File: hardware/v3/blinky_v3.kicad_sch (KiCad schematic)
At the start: 147 parts, among them J1 Conn_01x07, J2 Conn_01x03_Pin, J3 RJ45, J4 Conn_01x06_Pin, J5 Conn_01x05_Pin, J6 Conn_02x10_Counter_Clockwise, J7 Conn_01x04_Pin, J8 Conn_01x04_Pin, J9 Conn_01x06_Pin, Q1 2N7002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

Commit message: start routing
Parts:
- J6: now not fitted; now left out of the parts list
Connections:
- net OCXO_OUT: now reaches JP11.1 (A), JP13.1 (A), TP12.1, Y2.4 (RF_OUTPUT)
- net 10Mhz2.5V: now reaches C10.2, R25.2, R4.1, TP6.1, U14.6 (-), U4.3 (+)
- net 10MHz0v: now reaches C40.2, R38.1, TP21.1, U2.3 (+), U3.3 (+IN)
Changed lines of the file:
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@@
     (effects (font (size 1.27 1.27)) (justify left bottom))
   )
+  (label "OCXO_OUT" (at 86.36 259.08 0) (fields_autoplaced)
+    (effects (font (size 1.27 1.27)) (justify left bottom))
+  )
   (label "LEDM3" (at 312.42 55.88 0) (fields_autoplaced)
     (effects (font (size 1.27 1.27)) (justify left bottom))
   )
+  (label "10Mhz2.5V" (at 119.38 232.41 0) (fields_autoplaced)
+    (effects (font (size 1.27 1.27)) (justify left bottom))
+  )
   (label "LEDB" (at 312.42 86.36 0) (fields_autoplaced)
     (effects (font (size 1.27 1.27)) (justify left bottom))
@@
     (effects (font (size 1.27 1.27)) (justify left bottom))
   )
+  (label "10MHz0v" (at 119.38 281.94 0) (fields_autoplaced)
+    (effects (font (size 1.27 1.27)) (justify left bottom))
+  )
   (label "LEDE" (at 367.03 88.9 0) (fields_autoplaced)
     (effects (font (size 1.27 1.27)) (justify left bottom))
@@
     )
   )
-  (symbol (lib_id "Connector:TestPoint") (at 162.56 207.01 0) (unit 1)
+  (symbol (lib_id "Connector:TestPoint") (at 162.56 207.01 0) (mirror y) (unit 1)
     (in_bom yes) (on_board yes) (dnp no)
-    (property "Reference" "TP7" (at 161.29 201.93 0)
+    (property "Reference" "TP7" (at 163.83 201.93 0)
       (effects (font (size 1.27 1.27)) (justify left))
     )
-    (property "Value" "~" (at 161.29 200.66 0)
+    (property "Value" "~" (at 163.83 200.66 0)
       (effects (font (size 1.27 1.27)) (justify left))
     )
-    (property "Footprint" "TestPoint:TestPoint_THTPad_D1.5mm_Drill0.7mm" (at 167.64 207.01 0)
+    (property "Footprint" "TestPoint:TestPoint_THTPad_D1.5mm_Drill0.7mm" (at 157.48 207.01 0)
       (effects (font (size 1.27 1.27)) hide)
     )
-    (property "Datasheet" "~" (at 167.64 207.01 0)
+    (property "Datasheet" "~" (at 157.48 207.01 0)
       (effects (font (size 1.27 1.27)) hide)
     )
@@
   )
   (symbol (lib_id "Connector_Generic:Conn_02x10_Counter_Clockwise") (at 359.41 88.9 0) (unit 1)
-    (in_bom yes) (on_board yes) (dnp no) (fields_autoplaced)
+    (in_bom no) (on_board no) (dnp yes) (fields_autoplaced)
     (property "Reference" "J6" (at 360.68 72.39 0)
       (effects (font (size 1.27 1.27)))

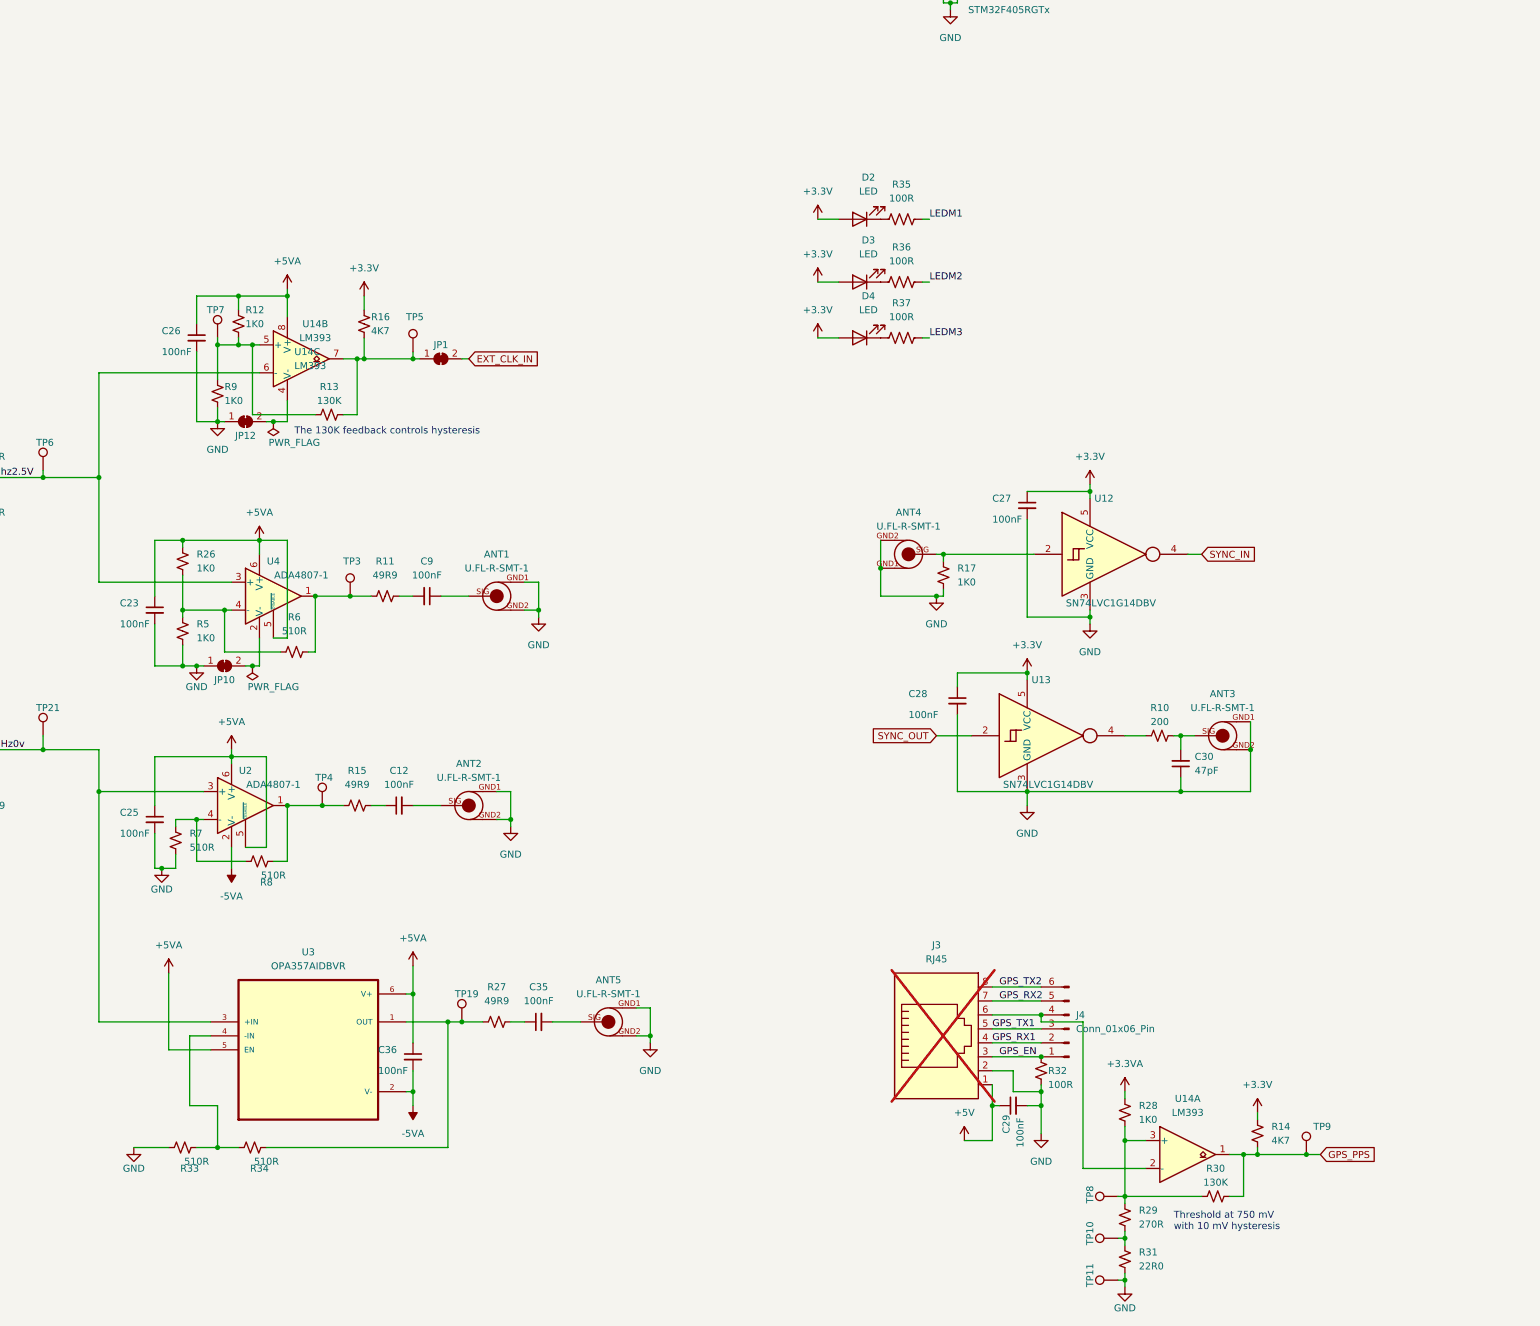
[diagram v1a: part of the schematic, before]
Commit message: update comparator and start routing
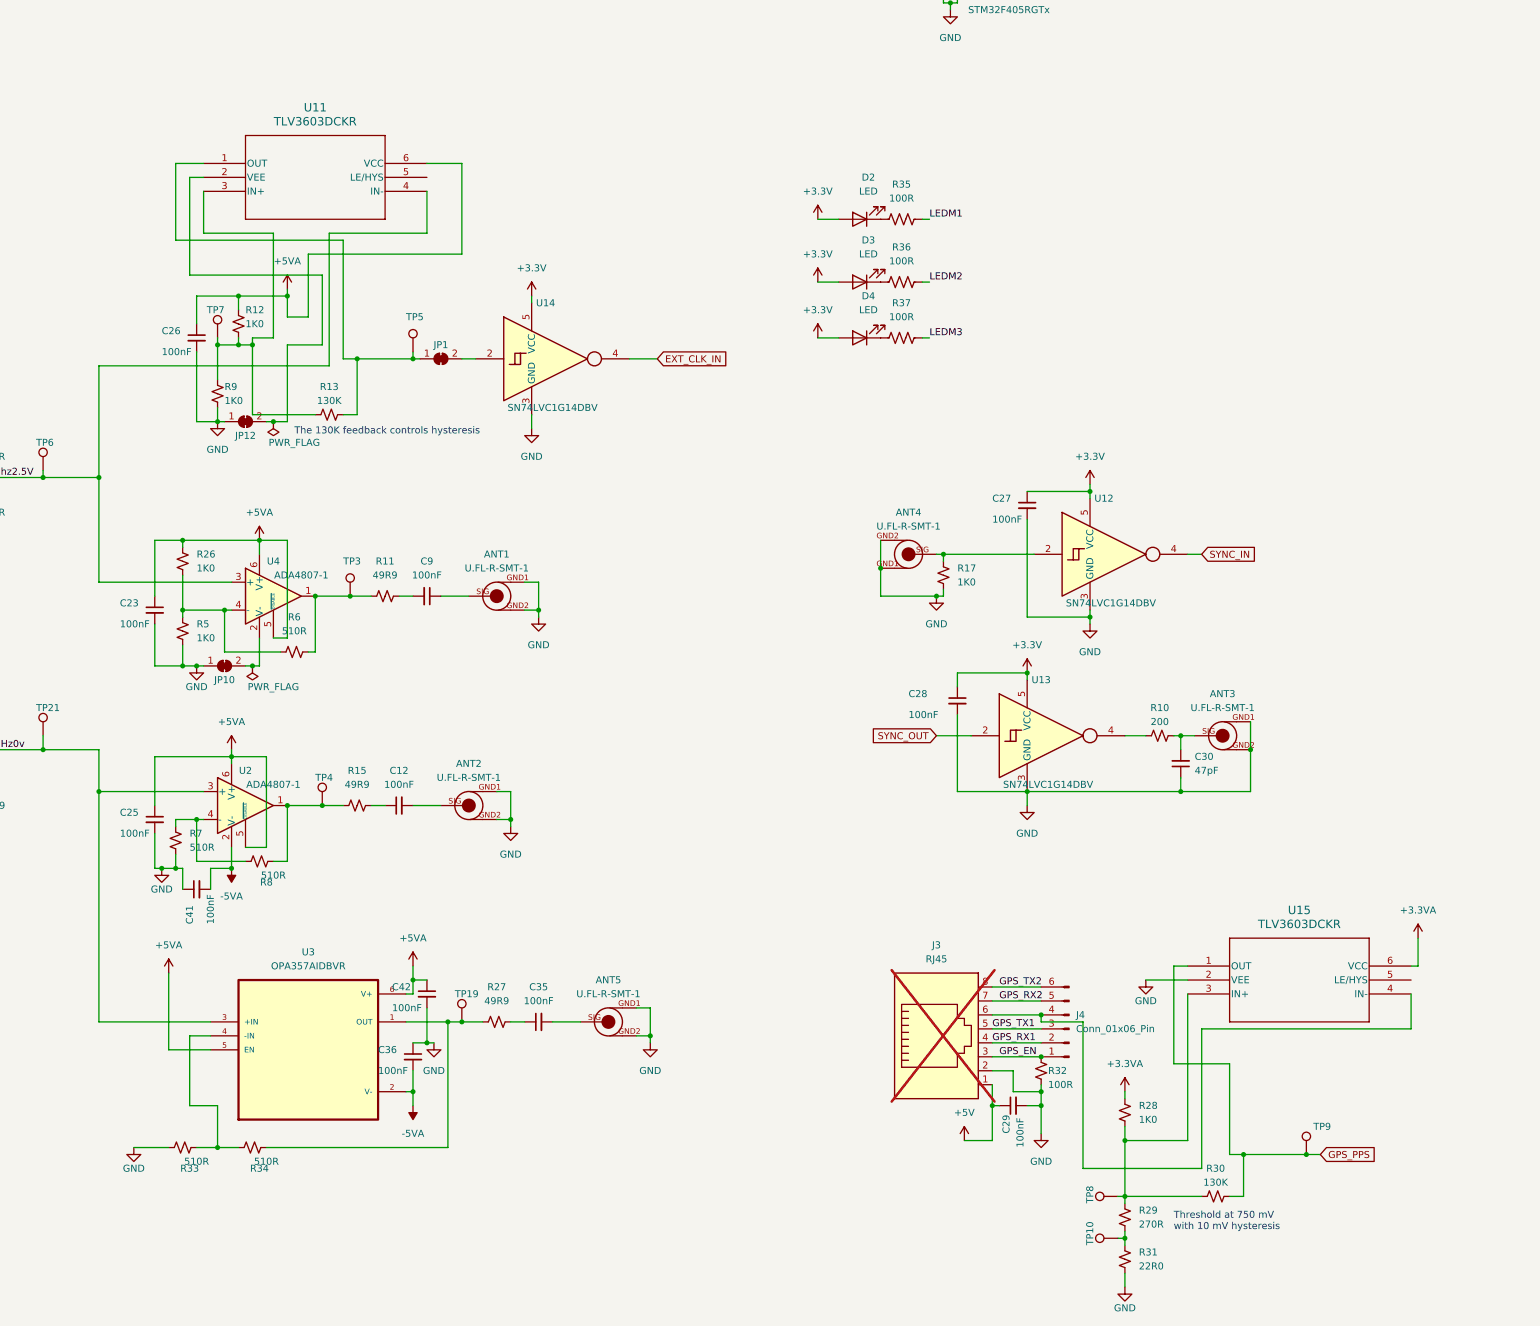
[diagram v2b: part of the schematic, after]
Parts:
- removed R14, R16: 4K7, Resistor_SMD:R_0603_1608Metric, symbol Device:R_Small_US
- removed TP11: ~, TestPoint:TestPoint_THTPad_D1.5mm_Drill0.7mm, symbol Connector:TestPoint
- removed U14: LM393, Package_SO:SOIC-8_3.9x4.9mm_P1.27mm, symbol Comparator:LM393
- added C41, C42: 100nF, Capacitor_SMD:C_0402_1005Metric, symbol Device:C_Small
- added U11, U15: TLV3603DCKR, SC70_DCK_TEX, symbol blinky:TLV3603DCKR
- added U14: SN74LVC1G14DBV, Package_TO_SOT_SMD:SOT-23-5, symbol 74xGxx:SN74LVC1G14DBV
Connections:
- net +3.3V: now also U14.5 (VCC)
- net +3.3VA: now also U15.6 (VCC)
- net +5VA: now also C42.1, U11.6 (VCC); no longer C36.1
- net -5VA: now also C41.2
- net 10Mhz2.5V: now also U11.4 (IN-)
- net EXT_CLK_IN: now also U14.4; no longer JP1.2 (B)
- net GND: now also C36.1, C41.1, C42.2, U14.3 (GND), U15.2 (VEE)
- net GPS_PPS: now also U15.1 (OUT)
- net at R12.2, R13.1, R9.1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: now also U11.3 (IN+)
- net at JP1.1 (A), R13.2, TP5.1: now also U11.1 (OUT)
- net at R28.2, R29.1, R30.1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: now also U15.3 (IN+)
- net at JP12.2 (B): now also U11.2 (VEE)
- net at J3.6, J4.4 (Pin_4): now also U15.4 (IN-)
- new net: JP1.2 (B), U14.2

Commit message: update
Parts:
- U11, U15: footprint SC70_DCK_TEX -> blinky_footprints:SC70_DCK_TEX
- U3: footprint SOT95P280X145-6N -> blinky_footprints:SOT95P280X145-6N
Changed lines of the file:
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@@
       (effects (font (size 1.524 1.524)))
     )
-    (property "Footprint" "SC70_DCK_TEX" (at 339.09 321.31 0)
+    (property "Footprint" "blinky_footprints:SC70_DCK_TEX" (at 339.09 321.31 0)
       (effects (font (size 1.27 1.27) italic) hide)
     )
@@
       (effects (font (size 1.27 1.27)))
     )
-    (property "Footprint" "SOT95P280X145-6N" (at 179.07 336.55 0)
+    (property "Footprint" "blinky_footprints:SOT95P280X145-6N" (at 179.07 336.55 0)
       (effects (font (size 1.27 1.27)) (justify bottom) hide)
     )
@@
       (effects (font (size 1.524 1.524)))
     )
-    (property "Footprint" "SC70_DCK_TEX" (at 160.02 175.26 0)
+    (property "Footprint" "blinky_footprints:SC70_DCK_TEX" (at 160.02 175.26 0)
       (effects (font (size 1.27 1.27) italic) hide)
     )

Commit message: fix errors
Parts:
- added JP14: SolderJumper_2_Bridged, Jumper:SolderJumper-2_P1.3mm_Bridged_RoundedPad1.0x1.5mm, symbol Jumper:SolderJumper_2_Bridged
- added R14, R16: 130K, Resistor_SMD:R_0603_1608Metric, symbol Device:R_Small_US
- R13: now not fitted; now left out of the parts list
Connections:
- net GND: now also JP14.2 (B), R14.2, R16.2; no longer U13.3 (GND)
- net at U15.5 (LE/HYS): now also R16.1
- net at U11.5 (LE/HYS): now also R14.1
- new net: JP14.1 (A), U13.3 (GND)

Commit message: fix most errors
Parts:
- R13: now fitted
- R19, R20, R21, R22: value 49R9 -> 1K0; LCSC C17720 -> C21190
- R30: now left out of the parts list
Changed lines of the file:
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@@
       (effects (font (size 1.27 1.27)) (justify left))
     )
-    (property "Value" "49R9" (at 40.64 256.54 0)
+    (property "Value" "1K0" (at 40.64 256.54 0)
       (effects (font (size 1.27 1.27)) (justify left))
     )
@@
       (effects (font (size 1.27 1.27)) hide)
     )
-    (property "LCSC" "C17720" (at 38.1 255.27 0)
+    (property "LCSC" "C21190" (at 38.1 255.27 0)
       (effects (font (size 1.27 1.27)) hide)
     )
@@
       (effects (font (size 1.27 1.27)) (justify left))
     )
-    (property "Value" "49R9" (at 40.64 273.05 0)
+    (property "Value" "1K0" (at 40.64 273.05 0)
       (effects (font (size 1.27 1.27)) (justify left))
     )
@@
       (effects (font (size 1.27 1.27)) hide)
     )
-    (property "LCSC" "C17720" (at 38.1 271.78 0)
+    (property "LCSC" "C21190" (at 38.1 271.78 0)
       (effects (font (size 1.27 1.27)) hide)
     )
@@
   )
   (symbol (lib_id "Device:R_Small_US") (at 344.17 363.22 90) (unit 1)
-    (in_bom yes) (on_board yes) (dnp no)
+    (in_bom no) (on_board yes) (dnp no)
     (property "Reference" "R30" (at 344.17 358.14 90)
       (effects (font (size 1.27 1.27)))
@@
   )
   (symbol (lib_id "Device:R_Small_US") (at 182.88 220.98 90) (unit 1)
-    (in_bom no) (on_board yes) (dnp yes)
+    (in_bom no) (on_board yes) (dnp no)
     (property "Reference" "R13" (at 182.88 215.9 90)
       (effects (font (size 1.27 1.27)))
@@
       (effects (font (size 1.27 1.27)) (justify left))
     )
-    (property "Value" "49R9" (at 40.64 280.67 0)
+    (property "Value" "1K0" (at 40.64 280.67 0)
       (effects (font (size 1.27 1.27)) (justify left))
     )
@@
       (effects (font (size 1.27 1.27)) hide)
     )
-    (property "LCSC" "C17720" (at 38.1 279.4 0)
+    (property "LCSC" "C21190" (at 38.1 279.4 0)
       (effects (font (size 1.27 1.27)) hide)
     )
@@
       (effects (font (size 1.27 1.27)) (justify left))
     )
-    (property "Value" "49R9" (at 40.64 248.92 0)
+    (property "Value" "1K0" (at 40.64 248.92 0)
       (effects (font (size 1.27 1.27)) (justify left))
     )
@@
       (effects (font (size 1.27 1.27)) hide)
     )
-    (property "LCSC" "C17720" (at 38.1 247.65 0)
+    (property "LCSC" "C21190" (at 38.1 247.65 0)
       (effects (font (size 1.27 1.27)) hide)
     )

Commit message: update JLCPCB numbers
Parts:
- U11, U15: LCSC (none) -> C5213955
- U3: LCSC (none) -> C139385
- U6: LCSC (none) -> C69527
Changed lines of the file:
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@@
       (effects (font (size 1.27 1.27) italic) hide)
     )
+    (property "LCSC" "C5213955" (at 339.09 321.31 0)
+      (effects (font (size 1.27 1.27)) hide)
+    )
     (pin "1")
     (pin "2")
@@
       (effects (font (size 1.27 1.27)) hide)
     )
+    (property "LCSC" "C69527" (at 469.9 264.16 0)
+      (effects (font (size 1.27 1.27)) hide)
+    )
     (pin "1")
     (pin "2")
@@
       (effects (font (size 1.27 1.27)) hide)
     )
+    (property "LCSC" "C139385" (at 179.07 336.55 0)
+      (effects (font (size 1.27 1.27)) hide)
+    )
     (pin "1")
     (pin "2")
@@
       (effects (font (size 1.27 1.27) italic) hide)
     )
+    (property "LCSC" "C5213955" (at 160.02 175.26 0)
+      (effects (font (size 1.27 1.27)) hide)
+    )
     (pin "1")

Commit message: update
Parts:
- added TP11, TP22, TP23, TP24: ~, TestPoint:TestPoint_THTPad_D1.5mm_Drill0.7mm, symbol Connector:TestPoint
- J7: now not fitted; now left out of the parts list
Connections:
- net -5VA: no longer TP18.1, TP20.1
- net SYNC_IN: now also TP22.1
- net SYNC_OUT: now also TP23.1
- net at J3.6, J4.4 (Pin_4), U15.4 (IN-): now also TP10.1
- net at R29.2, R31.1: no longer TP10.1
- net at C39.2, JP9.1 (A), U6.1 (VOUT): now also TP20.1
- net at R10.1, U13.4: now also TP24.1
- net at ANT4.SIG, R17.1, U12.2: now also TP11.1
- net at C16.2, JP5.1 (A), U9.3 (VO): now also TP18.1
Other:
- moved on the sheet: TP18, TP20

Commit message: update op amp for single supply
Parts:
- removed C36: 100nF, Capacitor_SMD:C_0402_1005Metric, symbol Device:C_Small
- added R39: 1K0, Resistor_SMD:R_0603_1608Metric, symbol Device:R_Small_US
- J1, J2, J4, J5, J8, J9, JP1, JP10, JP11, JP12, JP13, JP14, JP2, JP3, JP4, JP5, JP6, JP7, JP8, JP9: now not fitted; now left out of the parts list
- R10: value 200 -> 200R
- R33: value 510R -> 1K0; LCSC C23193 -> C21190
- TP12, TP21, TP6: value TestPoint -> ~; now not fitted; now left out of the parts list
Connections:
- net +5VA: now also R39.1
- net -5VA: no longer U3.2 (V-)
- net 10MHz0v: no longer U3.3 (+IN)
- net 10Mhz2.5V: now also U3.3 (+IN)
- net GND: now also U3.2 (V-)
- net at R33.2, R34.1, U3.4 (-IN): now also R39.2
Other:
- moved on the sheet: ANT2, ANT5, C12, C25, C35, C40, C41, C42, R15, R27, R33, R34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
